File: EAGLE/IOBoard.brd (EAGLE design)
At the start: 50 x 50 mm, 44 parts, among them IC1 TPS61097, Q1 8MHz, Q2 32kHz, U1 STM32F10XRXT6

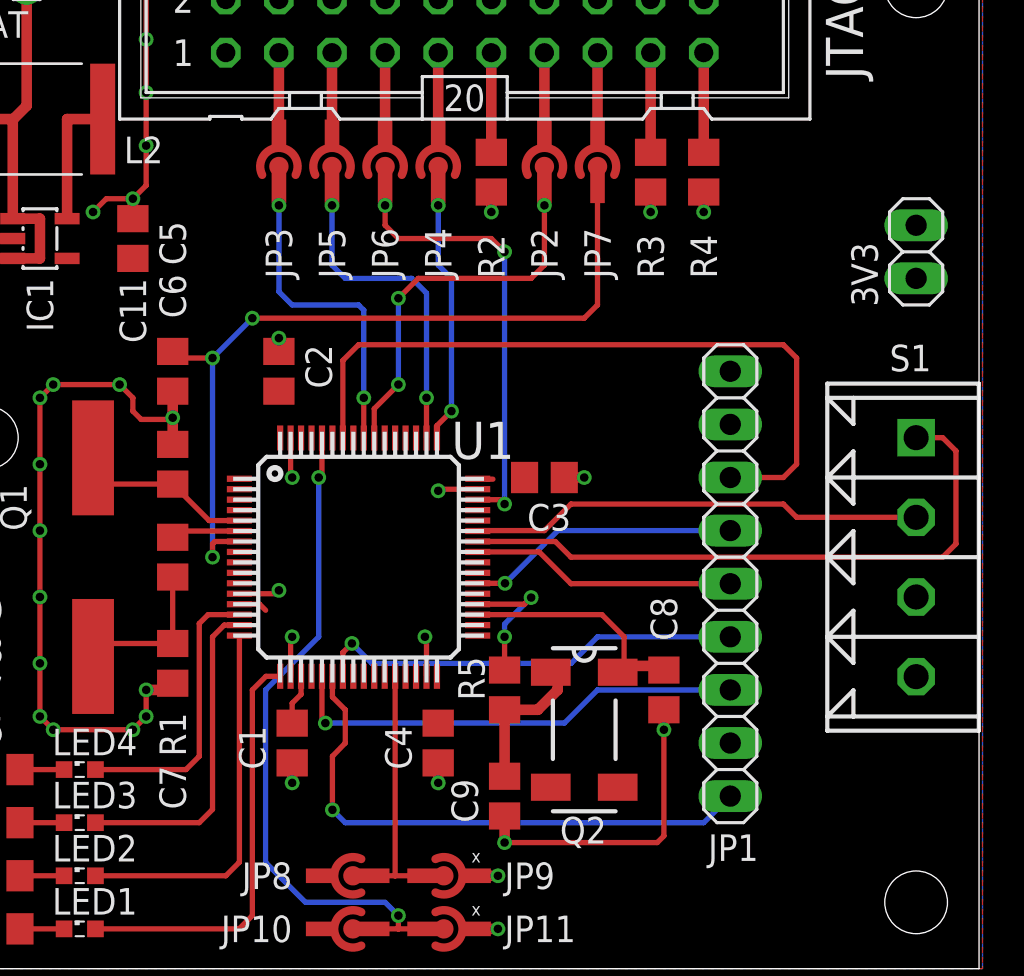
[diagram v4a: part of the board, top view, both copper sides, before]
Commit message: Finished first prototype of the circuit board
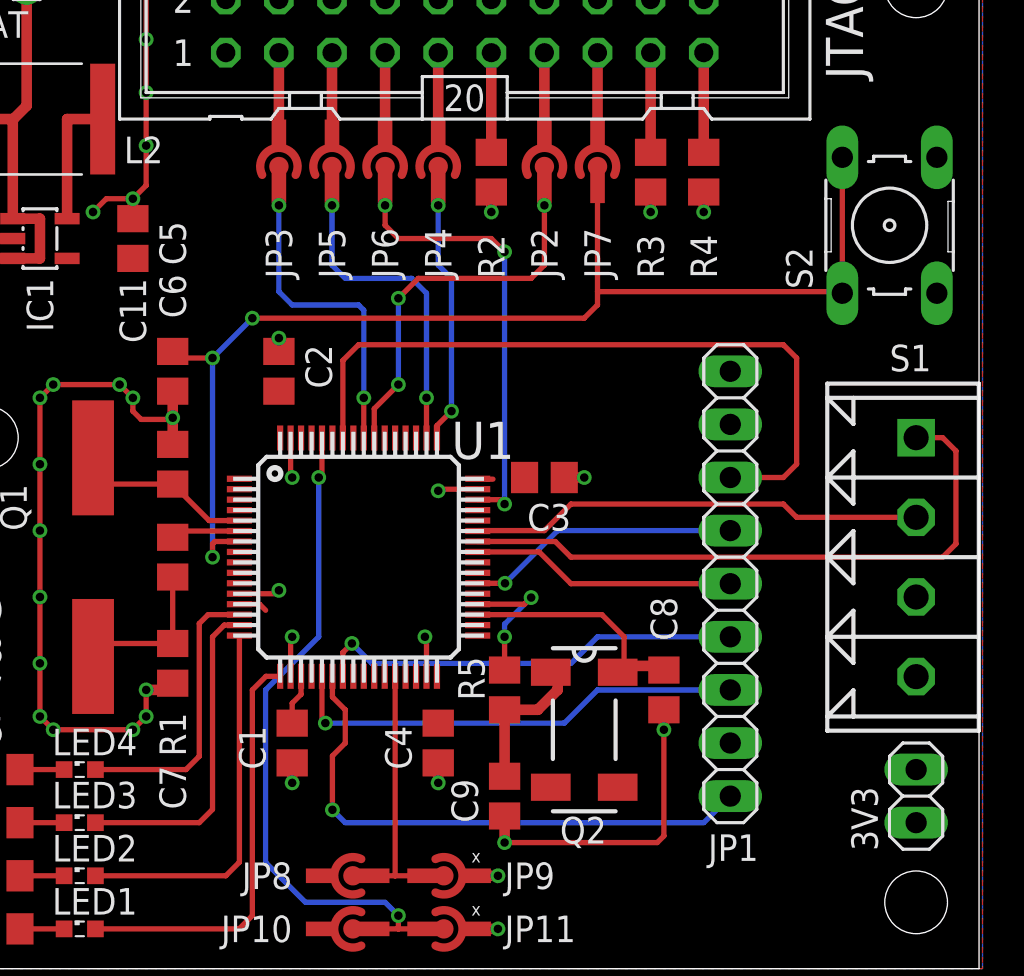
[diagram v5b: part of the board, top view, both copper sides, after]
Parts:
- added S2: (no value), switch-omron:B3F-10XX
- moved 3V3 26.0 mm to (47.0, 8.26)
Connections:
- net GND: now also S2.3, S2.4
- net N$1: now also S2.1, S2.2
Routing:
- net N$1: track 38.6 -> 56.9 mm
- net GND: vias 41 -> 42
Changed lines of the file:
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@@
 <?xml version="1.0" encoding="utf-8"?>
 <!DOCTYPE eagle SYSTEM "eagle.dtd">
-<eagle version="6.5.0">
+<eagle version="7.5.0">
 <drawing>
 <settings>
@@
 <setting verticaltext="up"/>
 </settings>
-<grid distance="25" unitdist="mil" unit="mm" style="lines" multiple="1" display="yes" altdistance="12.5" altunitdist="mil" altunit="mil"/>
+<grid distance="25" unitdist="mil" unit="mil" style="lines" multiple="1" display="yes" altdistance="12.5" altunitdist="mil" altunit="mil"/>
 <layers>
 <layer number="1" name="Top" color="4" fill="1" visible="yes" active="yes"/>
@@
 </class>
 </classes>
-<designrules name="ITead_rule">
+<designrules name="ITead_rule *">
 <description language="de">&lt;b&gt;EAGLE Design Rules&lt;/b&gt;
 &lt;p&gt;
@@
 <param name="dpGapFactor" value="2.5"/>
 <param name="checkGrid" value="0"/>
-<param name="checkAngle" value="0"/>
+<param name="checkAngle" value="1"/>
 <param name="checkFont" value="1"/>
 <param name="checkRestrict" value="0"/>
@@
 <pass name="Default">
 <param name="RoutingGrid" value="50mil"/>
+<param name="AutoGrid" value="1"/>
+<param name="Efforts" value="0"/>
+<param name="TopRouterVariant" value="1"/>
 <param name="tpViaShape" value="round"/>
 <param name="PrefDir.1" value="|"/>
@@
 <attribute name="NAME" x="27.305" y="1.27" size="1.27" layer="21"/>
 </element>
-<element name="3V3" library="pinhead" package="1X02" value="" x="46.99" y="34.29" rot="R90"/>
+<element name="3V3" library="pinhead" package="1X02" value="" x="46.99" y="8.255" rot="R90"/>
 <element name="BAT" library="pinhead" package="1X02" value="" x="3.175" y="47.625" smashed="yes" rot="R180">
 <attribute name="NAME" x="4.5212" y="45.7962" size="1.27" layer="25" ratio="10" rot="R180"/>
@@
 <attribute name="NAME" x="8.89" y="33.02" size="1.27" layer="25" rot="R270"/>
 <attribute name="VALUE" x="6.985" y="36.195" size="1.27" layer="27" rot="R270"/>
+</element>
+<element name="S2" library="switch-omron" package="B3F-10XX" value="" x="45.72" y="35.56" rot="R90">
+<attribute name="MPN" value="B3F-1000" x="45.72" y="35.56" size="1.778" layer="27" rot="R90" display="off"/>
+<attribute name="MF" value="" x="45.72" y="35.56" size="1.778" layer="27" rot="R90" display="off"/>
+<attribute name="OC_NEWARK" value="36M3542" x="45.72" y="35.56" size="1.778" layer="27" rot="R90" display="off"/>
+<attribute name="OC_FARNELL" value="176432" x="45.72" y="35.56" size="1.778" layer="27" rot="R90" display="off"/>
 </element>
 </elements>
@@
 <wire x1="34.925" y1="6.35" x2="34.925" y2="11.43" width="0.254" layer="1"/>
 <via x="5.08" y="17.78" extent="1-16" drill="0.4064"/>
+<via x="9.525" y="27.305" extent="1-16" drill="0.4064"/>
+<contactref element="S2" pad="4"/>
+<contactref element="S2" pad="3"/>
 </signal>
 <signal name="+3V3">
@@
 <contactref element="JP1" pad="1"/>
 <contactref element="U1" pad="22"/>
-<wire x1="19.07" y1="10.16" x2="19.685" y2="10.795" width="0.254" layer="1"/>
-<wire x1="19.685" y1="10.795" x2="19.685" y2="12.3825" width="0.254" layer="1"/>
 <wire x1="19.685" y1="12.3825" x2="19.07" y2="12.9975" width="0.254" layer="1"/>
 <wire x1="19.07" y1="12.9975" x2="19.07" y2="13.985" width="0.254" layer="1"/>
@@
 <wire x1="19.685" y1="6.985" x2="19.07" y2="7.6" width="0.254" layer="16"/>
 <via x="19.07" y="7.6" extent="1-16" drill="0.4064"/>
-<wire x1="19.07" y1="7.6" x2="19.07" y2="10.16" width="0.254" layer="1"/>
+<wire x1="19.685" y1="12.3825" x2="19.685" y2="10.795" width="0.254" layer="1"/>
+<wire x1="19.685" y1="10.795" x2="19.07" y2="10.18" width="0.254" layer="1"/>
+<wire x1="19.07" y1="10.18" x2="19.07" y2="7.6" width="0.254" layer="1"/>
 </signal>
 <signal name="LCD_SCK">
@@
 <via x="13.335" y="19.685" extent="1-16" drill="0.4064"/>
 <contactref element="JP7" pad="1"/>
-<wire x1="31.75" y1="37.37" x2="31.75" y2="31.75" width="0.254" layer="1"/>
+<wire x1="31.75" y1="37.37" x2="31.75" y2="32.385" width="0.254" layer="1"/>
+<wire x1="31.75" y1="32.385" x2="31.75" y2="31.75" width="0.254" layer="1"/>
 <wire x1="31.75" y1="31.75" x2="31.115" y2="31.115" width="0.254" layer="1"/>
 <wire x1="31.115" y1="31.115" x2="15.24" y2="31.115" width="0.254" layer="1"/>
@@
 <wire x1="13.335" y1="20.32" x2="13.45" y2="20.435" width="0.254" layer="1"/>
 <wire x1="13.45" y1="20.435" x2="14.62" y2="20.435" width="0.254" layer="1"/>
+<contactref element="S2" pad="2"/>
+<contactref element="S2" pad="1"/>
+<wire x1="43.4594" y1="38.8112" x2="43.4594" y2="32.3088" width="0.254" layer="1"/>
+<wire x1="43.4594" y1="32.3088" x2="43.3832" y2="32.385" width="0.254" layer="1"/>
+<wire x1="43.3832" y1="32.385" x2="31.75" y2="32.385" width="0.254" layer="1"/>
 </signal>
 <signal name="N$2">
